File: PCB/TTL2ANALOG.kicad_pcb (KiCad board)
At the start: 2 copper layers, 60.5 x 56.1 mm, 39 parts, among them J1 EGA/CGA, J2 Brown Fix, J3 CSync Inv., J4 Sync Type, J5 TTL Input, J6 Analog Out, J7 Barrel_Jack, U1 GAL20V8, U2 74LS244, U3 74LS244, U4 L7805

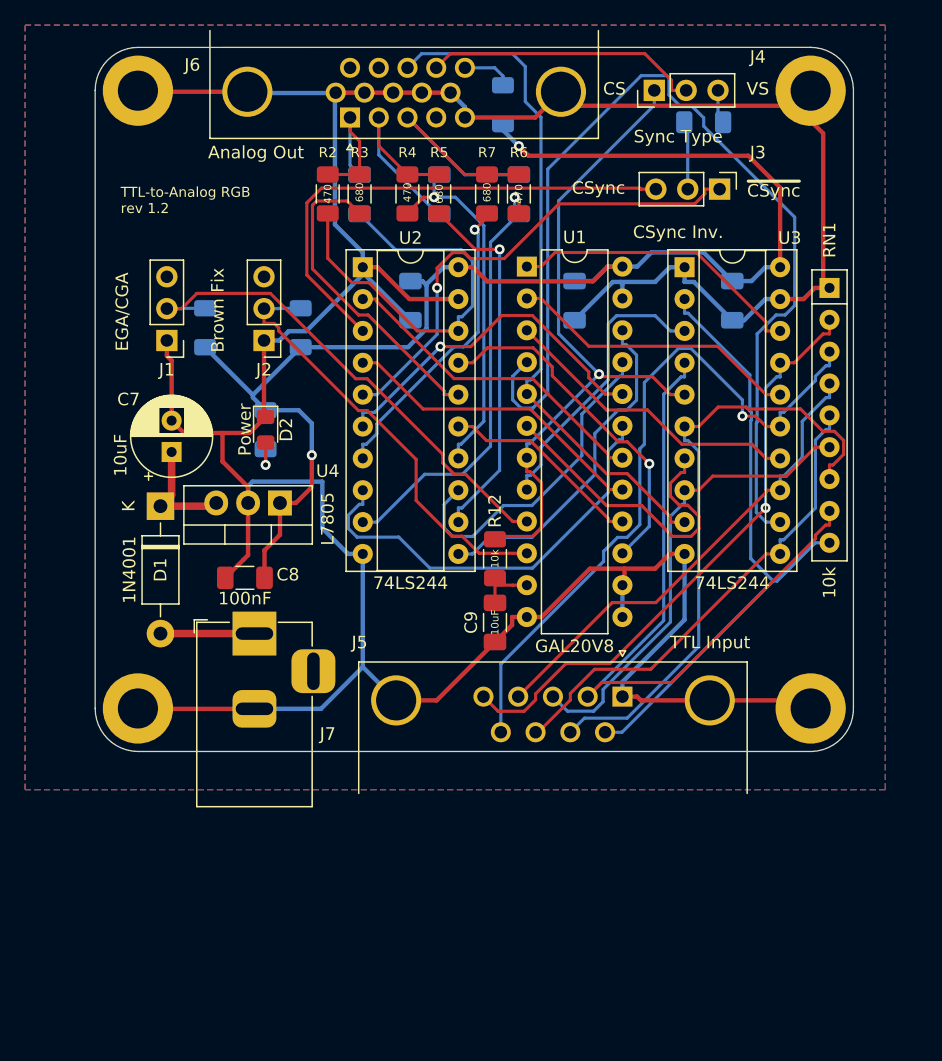
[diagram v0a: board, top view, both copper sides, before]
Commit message: Import to KiCad 7 and update the README with known issues
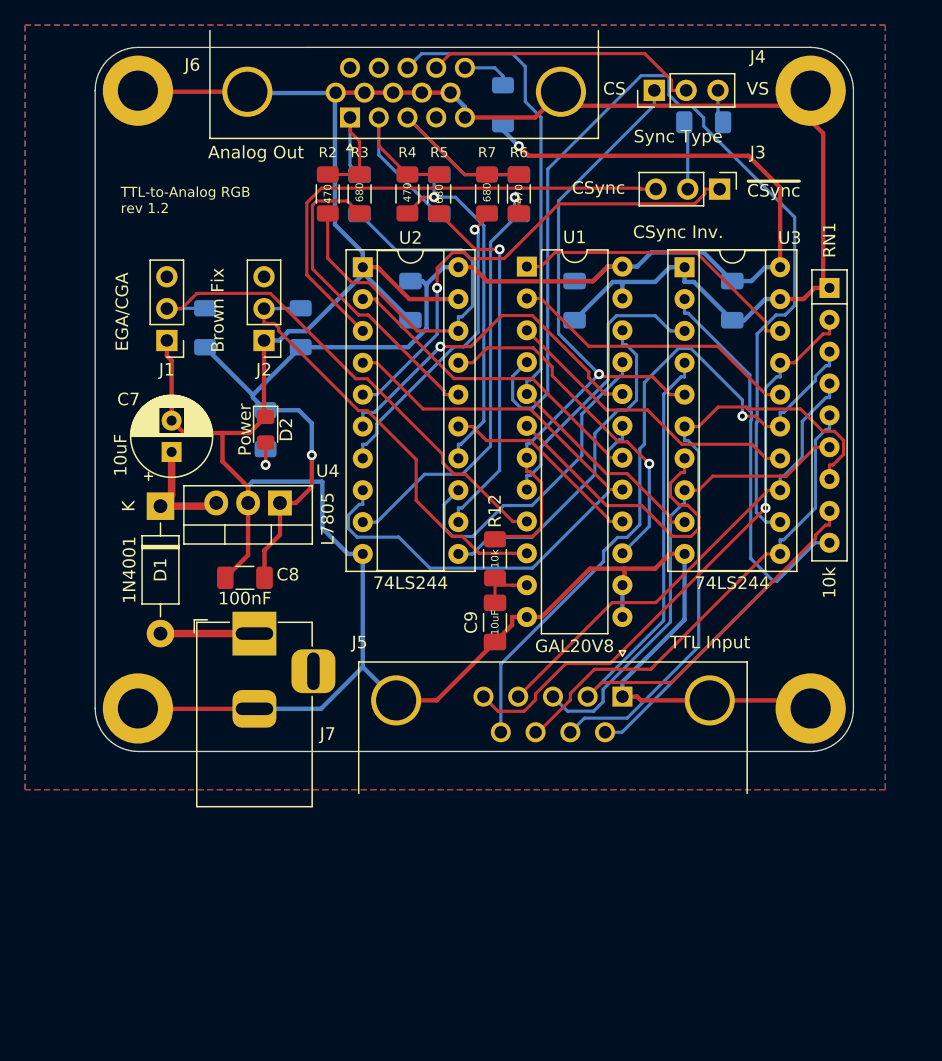
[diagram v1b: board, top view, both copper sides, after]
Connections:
- net /~DEC_CS renamed /~{DEC_CS}
- net /~OUT_CS renamed /~{OUT_CS}
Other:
- net class Default removed
- net class Power removed
- board text added: "~{CSync}"
- board text added: "~{SYNC}"
- board text removed: "~CSync"
- board text removed: "~SYNC"

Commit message: Redraw version 1.4
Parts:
- removed H1, H2, H3, H4: MountingHole_Pad, MountingHole:MountingHole_3.2mm_M3_DIN965_Pad
- removed J1: EGA/CGA, Connector_PinHeader_2.54mm:PinHeader_1x03_P2.54mm_Vertical
- removed R13: 0, Resistor_SMD:R_1206_3216Metric_Pad1.30x1.75mm_HandSolder
- removed R8, R9: 10k, Resistor_SMD:R_1206_3216Metric_Pad1.30x1.75mm_HandSolder
- removed U4: L7805, Package_TO_SOT_THT:TO-220-3_Vertical
- added JP1: 5V on video, Connector_PinHeader_2.54mm:PinHeader_1x02_P2.54mm_Vertical, F.Cu at (123.1, 74.1)
- added RN2: 10k, Resistor_THT:R_Array_SIP6, F.Cu at (130.3, 85.1)
- added U5: AMS1117-5.0, Package_TO_SOT_SMD:SOT-223-3_TabPin2, F.Cu at (129.7, 104.5)
- C7: footprint Capacitor_THT:CP_Radial_D6.3mm_P2.50mm -> Capacitor_SMD:C_1206_3216Metric_Pad1.33x1.80mm_HandSolder
- C8: value 100nF -> 10uF
- C9, R12, R3, R5, R7: moved to B.Cu
- D2: footprint LED_SMD:LED_0805_2012Metric_Pad1.15x1.40mm_HandSolder -> LED_SMD:LED_1206_3216Metric_Pad1.42x1.75mm_HandSolder
- J2: value Brown Fix -> Options; footprint Connector_PinHeader_2.54mm:PinHeader_1x03_P2.54mm_Vertical -> Connector_PinHeader_2.54mm:PinHeader_2x05_P2.54mm_Vertical
- moved RN1 46.9 mm to (143.9, 110.7), turned to 0 degrees
- moved U2 37.4 mm to (164.4, 78.3), turned to -90 degrees
- moved U3 33.9 mm to (164.4, 99.9), turned to -90 degrees
- moved C5 33.8 mm to (153.0, 103.7), turned to 180 degrees
- moved C7 32.4 mm to (134.8, 106.5)
- moved U1 31.5 mm to (164.4, 89.2), turned to -90 degrees
- moved D1 31.3 mm to (132.3, 110.8), turned to 180 degrees
- moved D2 26.0 mm to (122.0, 106.5), turned to 90 degrees
- moved R11 26.0 mm to (122.0, 106.5), turned to -90 degrees
- moved J2 25.0 mm to (126.8, 97.7)
- moved C6 23.8 mm to (153.0, 82.1), turned to 180 degrees
- moved C4 23.4 mm to (150.5, 93.0), turned to 180 degrees
- moved J4 22.3 mm to (144.8, 74.7)
- moved J7 19.1 mm to (125.5, 115.0)
- moved R10 18.8 mm to (153.4, 74.7), turned to 180 degrees
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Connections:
- J2 pad 1: GND -> Net-(J2-Pin_1)
- J2 pad 2: /BRWN_FIX -> VCC
- J2 pad 3: (no net) -> Net-(J2-Pin_3)
- J6 pad 11: (no net) -> unconnected-(J6-Pad11)
- J6 pad 12: (no net) -> unconnected-(J6-Pad12)
- J6 pad 15: Net-(J6-Pad15) -> unconnected-(J6-Pad15)
- J6 pad 4: (no net) -> unconnected-(J6-Pad4)
- J6 pad 9: GND -> Net-(JP1-B)
- RN1 pad 2: /IN_B -> /IN_HS
- RN1 pad 3: /IN_VS -> /IN_G
- RN1 pad 4: /IN_G -> /IN_VS
- RN1 pad 5: /IN_HS -> /IN_B
- U1 pad 13: GND -> Net-(J2-Pin_1)
- U1 pad 14: GND -> Net-(J2-Pin_3)
- U1 pad 23: GND -> Net-(J2-Pin_9)
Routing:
- net GND: track 281.2 -> 413.0 mm, vias 0 -> 90
- net /IN_R_BUF: track 81.0 -> 26.6 mm
- net Net-(J2-Pin_9): track 0.00 -> 50.6 mm
- net Net-(JP1-B): track 0.00 -> 35.5 mm
- net /IN_VS: track 56.3 -> 20.9 mm, vias 1 -> 0
- net /~{OUT_CS}: track 40.4 -> 5.48 mm
- net /OUT_CS: track 38.9 -> 6.02 mm, vias 1 -> 0
- net /OUT_B: track 35.0 -> 5.92 mm
- net VCC: track 113.4 -> 139.3 mm, vias 2 -> 6
- net /IN_B: track 48.2 -> 22.7 mm, vias 1 -> 0
- net /IN_R_I: track 56.2 -> 31.2 mm
- net /IN_G: track 38.3 -> 13.3 mm
- net /DEC_R_I: track 25.0 -> 47.9 mm, vias 0 -> 4
- net /IN_HS: track 38.7 -> 18.5 mm
- net /BRWN_FIX: track 34.7 -> 16.3 mm
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- added copper zone on In1.Cu, net GND
- added copper zone on In2.Cu, net VCC
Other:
- board size 60.5 x 56.1 mm -> 47 x 62.2 mm
- copper layers 2 -> 4
- board text added: "TTL-to-Analog RGB rev 1.4"
- board text removed: "CS"
- board text removed: "CSync"
- board text removed: "TTL-to-Analog RGB rev 1.2"
- board text removed: "VS"
- board text removed: "~{CSync}"
- board text removed: "~{SYNC}"

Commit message: Create gerbers for rev 1.4
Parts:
- C1, C2, C3: value 22pF -> 22p
- C7, C8, C9: value 10uF -> 10u
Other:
- board text added: "5V Enable"
- board text added: "BRWNFIX"
- board text added: "MODE"
- board text added: "OPT_1"
- board text added: "OPT_2"
- board text added: "OPT_3"
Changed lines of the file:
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@@
 			(drillshape 0)
 			(scaleselection 1)
-			(outputdirectory "gerbers/rev11")
+			(outputdirectory "gerbers/rev14")
 		)
 	)
@@
 		)
 		(property "Value" "CSync Inv."
-			(at 3.429 3.302 0)
+			(at 2.813 3.302 0)
 			(layer "F.SilkS")
-			(hide yes)
 			(effects
 				(font
@@
 			)
 		)
-		(property "Value" "10uF"
+		(property "Value" "10u"
 			(at 0 0 90)
 			(layer "F.SilkS")
@@
 				(font
 					(size 0.6 0.6)
-					(thickness 0.15)
+					(thickness 0.1)
+					(bold yes)
 				)
 			)
@@
 			)
 		)
-		(property "Value" "10uF"
+		(property "Value" "10u"
 			(at 0 0 90)
 			(layer "F.SilkS")
@@
 				(font
 					(size 0.6 0.6)
-					(thickness 0.15)
+					(thickness 0.1)
+					(bold yes)
 				)
 			)
@@
 				(font
 					(size 0.6 0.6)
-					(thickness 0.15)
+					(thickness 0.1)
+					(bold yes)
 				)
 				(justify mirror)
@@
 		(tags "resistor handsolder")
 		(property "Reference" "R5"
-			(at 3.302 0 0)
+			(at -3.3333 0 0)
 			(layer "B.SilkS")
 			(effects
@@
 				(font
 					(size 0.6 0.6)
-					(thickness 0.15)
+					(thickness 0.1)
+					(bold yes)
 				)
 				(justify mirror)
@@
 		(tags "resistor handsolder")
 		(property "Reference" "R7"
-			(at 3.302 0 0)
+			(at -3.4133 0 0)
 			(layer "B.SilkS")
 			(effects
@@
 				(font
 					(size 0.6 0.6)
-					(thickness 0.15)
+					(thickness 0.1)
+					(bold yes)
 				)
 				(justify mirror)
@@
 		(tags "resistor handsolder")
 		(property "Reference" "R11"
-			(at 3.95 0 90)
+			(at -4.915 0 90)
 			(layer "B.SilkS")
 			(effects
@@
 		)
 		(property "Value" "1-4.7k"
-			(at 0 -1.397 90)
+			(at 0 -1.59 90)
 			(layer "B.SilkS")
 			(effects
@@
 		(tags "capacitor handsolder")
 		(property "Reference" "C1"
-			(at 3.332 0 0)
+			(at -3.3033 0 0)
 			(layer "B.SilkS")
 			(effects
@@
 			)
 		)
-		(property "Value" "22pF"
-			(at 0 0 -90)
+		(property "Value" "22p"
+			(at 0 0 270)
 			(layer "B.SilkS")
 			(effects
 				(font
 					(size 0.6 0.6)
-					(thickness 0.15)
+					(thickness 0.1)
+					(bold yes)
 				)
 				(justify mirror)
@@
 			)
 		)
-		(property "Value" "22pF"
+		(property "Value" "22p"
 			(at 0 0 90)
 			(layer "B.SilkS")
@@
 				(font
 					(size 0.6 0.6)
-					(thickness 0.15)
+					(thickness 0.1)
+					(bold yes)
 				)
 				(justify mirror)
@@
 		(tags "capacitor handsolder")
 		(property "Reference" "C3"
-			(at 3.332 0 180)
+			(at -3.3833 0 180)
 			(layer "B.SilkS")
 			(effects
@@
 			)
 		)
-		(property "Value" "22pF"
+		(property "Value" "22p"
 			(at 0 0 90)
 			(layer "B.SilkS")
@@
 				(font
 					(size 0.6 0.6)
-					(thickness 0.15)
+					(thickness 0.1)
+					(bold yes)
 				)
 				(justify mirror)
@@
 			)
 		)
-		(property "Value" "10uF"
+		(property "Value" "10u"
 			(at 0 0 0)
 			(layer "B.SilkS")
@@
 				(font
 					(size 0.6 0.6)
-					(thickness 0.15)
+					(thickness 0.1)
+					(bold yes)
 				)
 				(justify mirror)
@@
 		(layer "Edge.Cuts")
 	)
+	(gr_text "MODE"
+		(at 122.682 92.595 0)
+		(layer "F.SilkS")
+		(effects
+			(font
+				(size 0.6 0.4)
+				(thickness 0.1)
+			)
+			(justify right)
+		)
+	)
+	(gr_text "OPT_3"
+		(at 122.428 97.79 0)
+		(layer "F.SilkS")
+		(effects
+			(font
+				(size 0.6 0.4)
+				(thickness 0.1)
+			)
+			(justify right)
+		)
+	)
+	(gr_text "OPT_1"
+		(at 122.682 87.63 0)
+		(layer "F.SilkS")
+		(effects
+			(font
+				(size 0.6 0.4)
+				(thickness 0.1)
+			)
+			(justify right)
+		)
+	)
+	(gr_text "5V Enable"
+		(at 124.206 71.628 0)
+		(layer "F.SilkS")
+		(effects
+			(font
+				(size 0.7 0.7)
+				(thickness 0.1)
+			)
+		)
+	)
 	(gr_text "TTL-to-Analog RGB\nrev 1.4"
 		(at 120.904 79.756 0)
@@
 		)
 	)
+	(gr_text "OPT_2"
+		(at 122.428 95.25 0)
+		(layer "F.SilkS")
+		(effects
+			(font
+				(size 0.6 0.4)
+				(thickness 0.1)
+			)
+			(justify right)
+		)
+	)
+	(gr_text "BRWNFIX"
+		(at 122.682 90.17 0)
+		(layer "F.SilkS")
+		(effects
+			(font
+				(size 0.6 0.4)
+				(thickness 0.1)
+			)
+			(justify right)
+		)
+	)
